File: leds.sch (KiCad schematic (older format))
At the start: 218 parts, among them U10 TLC5955, U11 TLC5955, U12 TLC5955, U13 TLC5955, U14 TLC5955, U15 TLC5955, U4 TLC5955, U5 TLC5955, U6 TLC5955, U7 TLC5955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

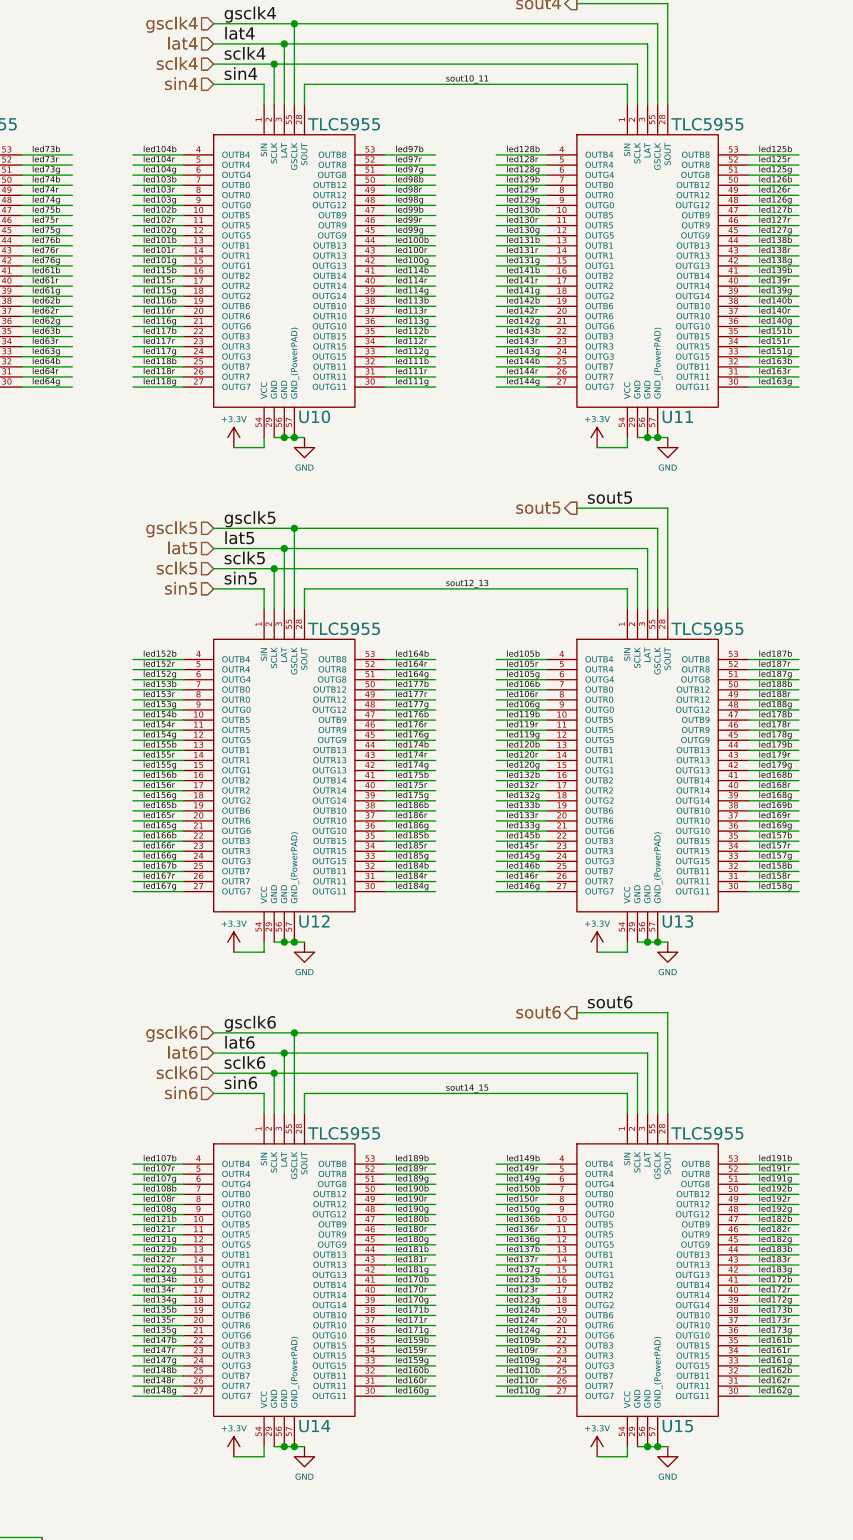
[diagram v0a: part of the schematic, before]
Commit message: Fix LED-mapping for lower half to match upper half.
(In schematics and netlist).
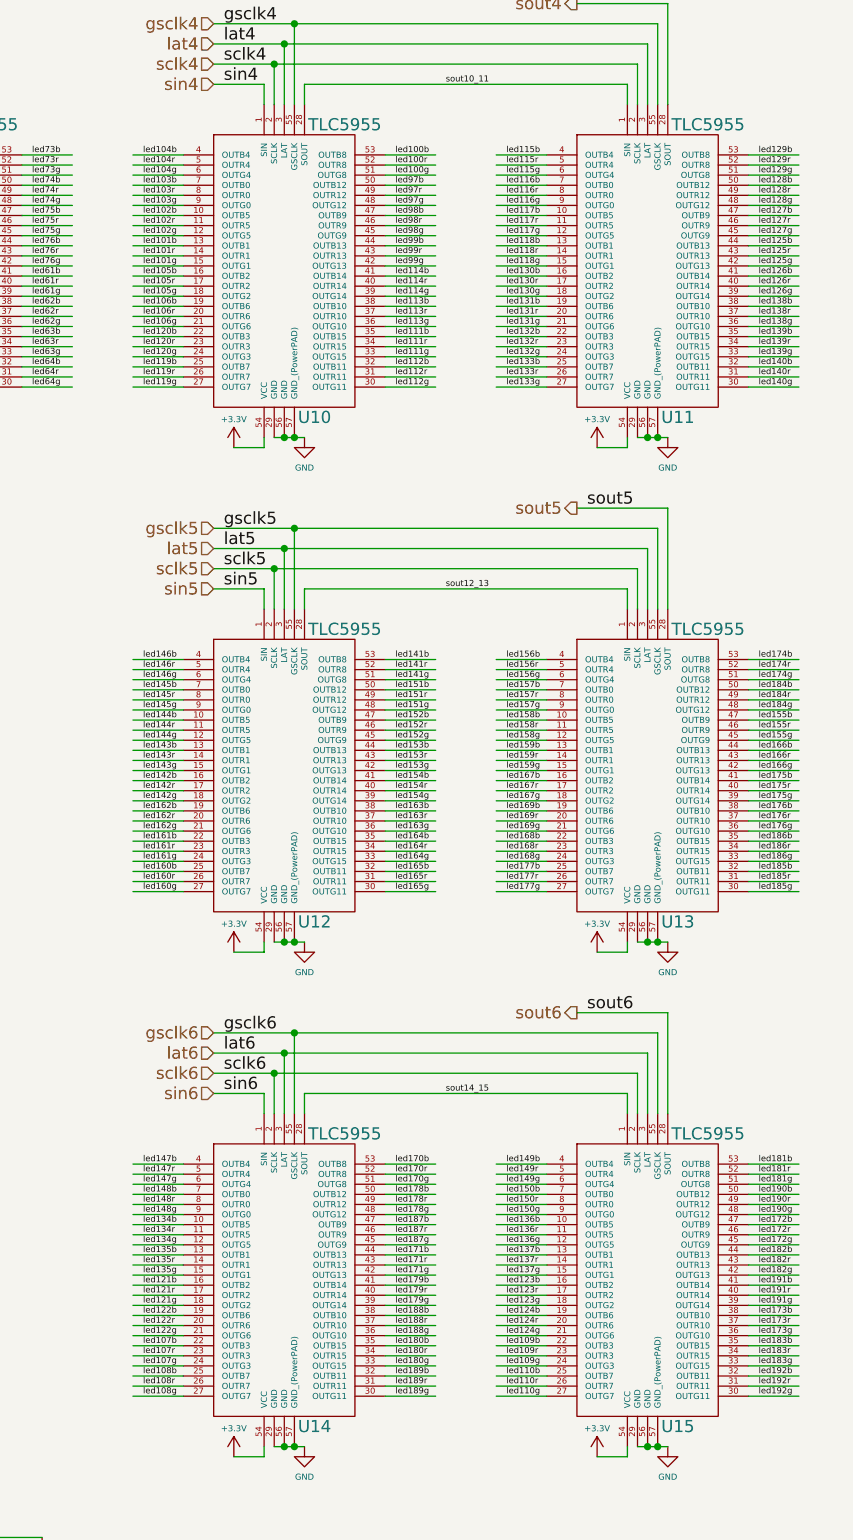
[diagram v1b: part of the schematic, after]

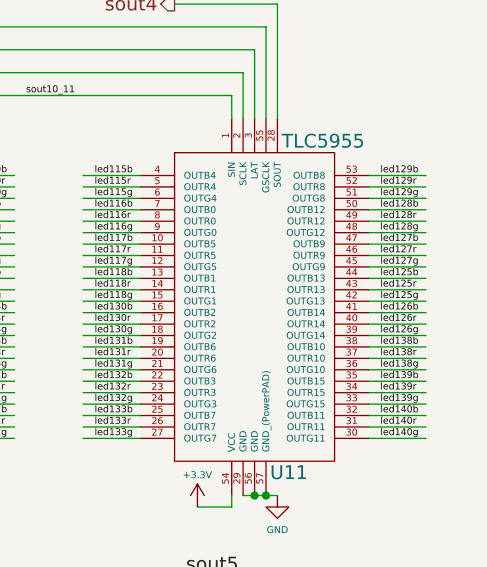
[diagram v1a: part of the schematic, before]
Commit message: Back TLC part of lower half of LEDs routed.
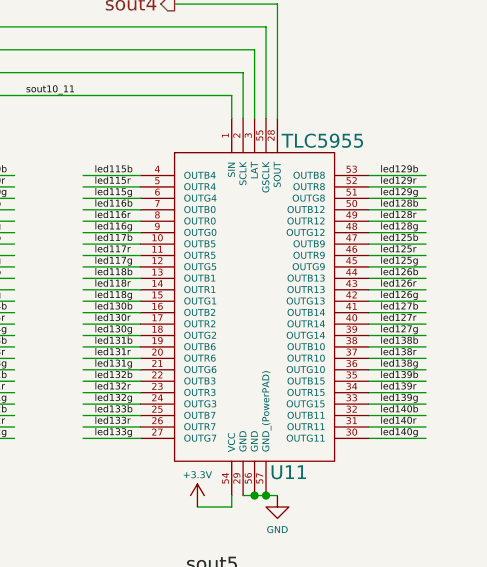
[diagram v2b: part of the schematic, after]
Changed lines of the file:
@@
 led138g
+Wire Wire Line
+	15550 2350 15300 2350
+Wire Wire Line
+	15550 2400 15300 2400
+Wire Wire Line
+	14300 2450 14050 2450
+Text Label 15350 2350 0    30   ~ 0
+led126b
+Text Label 15350 2400 0    30   ~ 0
+led126r
+Text Label 15350 2450 0    30   ~ 0
+led126g
+Wire Wire Line
+	15550 2200 15300 2200
+Wire Wire Line
+	15550 2250 15300 2250
+Wire Wire Line
+	14300 2600 14050 2600
+Text Label 15350 2200 0    30   ~ 0
+led125b
+Text Label 15350 2250 0    30   ~ 0
+led125r
+Text Label 15350 2300 0    30   ~ 0
+led125g
 Wire Wire Line
 	15550 2500 15300 2500
@@
 	15550 2550 15300 2550
 Wire Wire Line
-	14300 2450 14050 2450
+	14300 2750 14050 2750
 Text Label 15350 2500 0    30   ~ 0
-led126b
+led127b
 Text Label 15350 2550 0    30   ~ 0
-led126r
+led127r
 Text Label 15350 2600 0    30   ~ 0
-led126g
-Wire Wire Line
-	15550 2350 15300 2350
-Wire Wire Line
-	15550 2400 15300 2400
-Wire Wire Line
-	14300 2600 14050 2600
-Text Label 15350 2350 0    30   ~ 0
-led125b
-Text Label 15350 2400 0    30   ~ 0
-led125r
-Text Label 15350 2450 0    30   ~ 0
-led125g
-Wire Wire Line
-	15550 2200 15300 2200
-Wire Wire Line
-	15550 2250 15300 2250
-Wire Wire Line
-	14300 2750 14050 2750
-Text Label 15350 2200 0    30   ~ 0
-led127b
-Text Label 15350 2250 0    30   ~ 0
-led127r
-Text Label 15350 2300 0    30   ~ 0
 led127g
 Wire Wire Line

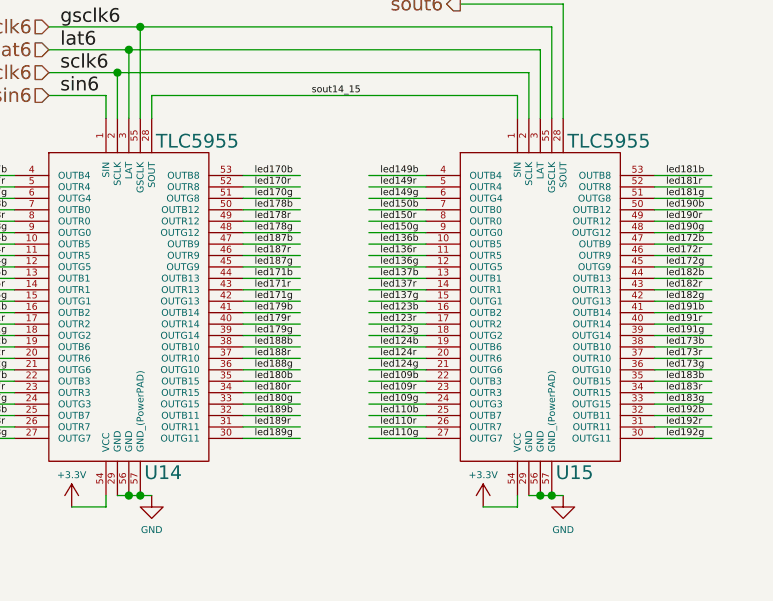
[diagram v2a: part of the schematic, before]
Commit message: Complete routing of LEDs.
Probably a good idea to do some additional cleanup, but it seems
already reasonable.
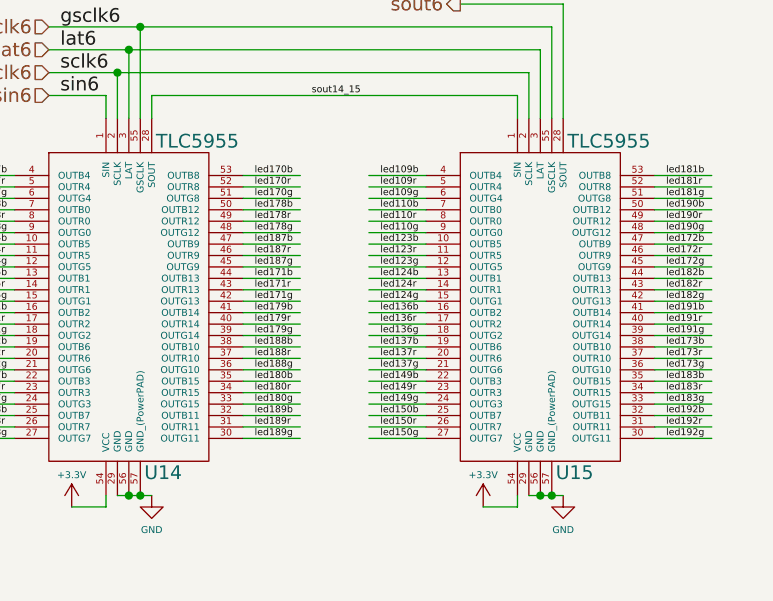
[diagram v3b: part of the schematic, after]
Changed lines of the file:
@@
 $EndComp
+Wire Wire Line
+	14300 7800 14050 7800
+Wire Wire Line
+	14300 7850 14050 7850
+Wire Wire Line
+	14300 7900 14050 7900
+Text Label 14100 7800 0    30   ~ 0
+led149b
+Text Label 14100 7850 0    30   ~ 0
+led149r
+Text Label 14100 7900 0    30   ~ 0
+led149g
+Wire Wire Line
+	14300 7950 14050 7950
+Wire Wire Line
+	14300 8000 14050 8000
+Wire Wire Line
+	14300 7150 14050 7150
+Text Label 14100 7950 0    30   ~ 0
+led150b
+Text Label 14100 8000 0    30   ~ 0
+led150r
+Text Label 14100 8050 0    30   ~ 0
+led150g
+Wire Wire Line
+	14300 7500 14050 7500
+Wire Wire Line
+	14300 7550 14050 7550
+Wire Wire Line
+	14300 7600 14050 7600
+Text Label 14100 7500 0    30   ~ 0
+led136b
+Text Label 14100 7550 0    30   ~ 0
+led136r
+Text Label 14100 7600 0    30   ~ 0
+led136g
+Wire Wire Line
+	14300 7650 14050 7650
+Wire Wire Line
+	14300 7700 14050 7700
+Wire Wire Line
+	14300 7450 14050 7450
+Text Label 14100 7650 0    30   ~ 0
+led137b
+Text Label 14100 7700 0    30   ~ 0
+led137r
+Text Label 14100 7750 0    30   ~ 0
+led137g
+Wire Wire Line
+	14300 7200 14050 7200
+Wire Wire Line
+	14300 7250 14050 7250
+Wire Wire Line
+	14300 7300 14050 7300
+Text Label 14100 7200 0    30   ~ 0
+led123b
+Text Label 14100 7250 0    30   ~ 0
+led123r
+Text Label 14100 7300 0    30   ~ 0
+led123g
+Wire Wire Line
+	14300 7350 14050 7350
+Wire Wire Line
+	14300 7400 14050 7400
+Wire Wire Line
+	14300 7750 14050 7750
+Text Label 14100 7350 0    30   ~ 0
+led124b
+Text Label 14100 7400 0    30   ~ 0
+led124r
+Text Label 14100 7450 0    30   ~ 0
+led124g
 Wire Wire Line
 	14300 6900 14050 6900
@@
 	14300 7000 14050 7000
 Text Label 14100 6900 0    30   ~ 0
-led149b
+led109b
 Text Label 14100 6950 0    30   ~ 0
-led149r
+led109r
 Text Label 14100 7000 0    30   ~ 0
-led149g
+led109g
 Wire Wire Line
 	14300 7050 14050 7050
@@
 	14300 7100 14050 7100
 Wire Wire Line
-	14300 7150 14050 7150
+	14300 8050 14050 8050
 Text Label 14100 7050 0    30   ~ 0
-led150b
+led110b
 Text Label 14100 7100 0    30   ~ 0
-led150r
+led110r
 Text Label 14100 7150 0    30   ~ 0
-led150g
-Wire Wire Line
-	14300 7200 14050 7200
-Wire Wire Line
-	14300 7250 14050 7250
-Wire Wire Line
-	14300 7300 14050 7300
-Text Label 14100 7200 0    30   ~ 0
-led136b
-Text Label 14100 7250 0    30   ~ 0
-led136r
-Text Label 14100 7300 0    30   ~ 0
-led136g
-Wire Wire Line
-	14300 7350 14050 7350
-Wire Wire Line
-	14300 7400 14050 7400
-Wire Wire Line
-	14300 7450 14050 7450
-Text Label 14100 7350 0    30   ~ 0
-led137b
-Text Label 14100 7400 0    30   ~ 0
-led137r
-Text Label 14100 7450 0    30   ~ 0
-led137g
-Wire Wire Line
-	14300 7500 14050 7500
-Wire Wire Line
-	14300 7550 14050 7550
-Wire Wire Line
-	14300 7600 14050 7600
-Text Label 14100 7500 0    30   ~ 0
-led123b
-Text Label 14100 7550 0    30   ~ 0
-led123r
-Text Label 14100 7600 0    30   ~ 0
-led123g
-Wire Wire Line
-	14300 7650 14050 7650
-Wire Wire Line
-	14300 7700 14050 7700
-Wire Wire Line
-	14300 7750 14050 7750
-Text Label 14100 7650 0    30   ~ 0
-led124b
-Text Label 14100 7700 0    30   ~ 0
-led124r
-Text Label 14100 7750 0    30   ~ 0
-led124g
-Wire Wire Line
-	14300 7800 14050 7800
-Wire Wire Line
-	14300 7850 14050 7850
-Wire Wire Line
-	14300 7900 14050 7900
-Text Label 14100 7800 0    30   ~ 0
-led109b
-Text Label 14100 7850 0    30   ~ 0
-led109r
-Text Label 14100 7900 0    30   ~ 0
-led109g
-Wire Wire Line
-	14300 7950 14050 7950
-Wire Wire Line
-	14300 8000 14050 8000
-Wire Wire Line
-	14300 8050 14050 8050
-Text Label 14100 7950 0    30   ~ 0
-led110b
-Text Label 14100 8000 0    30   ~ 0
-led110r
-Text Label 14100 8050 0    30   ~ 0
 led110g
 Wire Wire Line

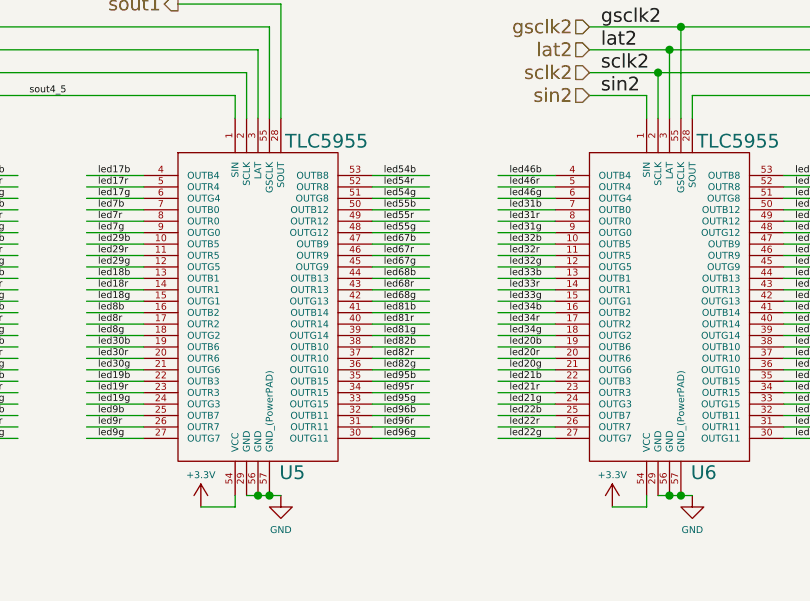
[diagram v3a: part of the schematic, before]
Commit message: Some cleanup of the LED routing.
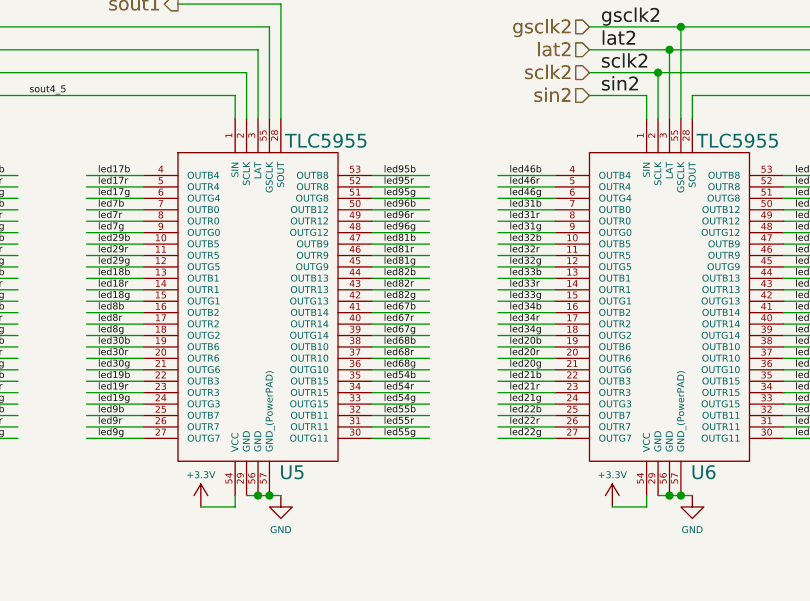
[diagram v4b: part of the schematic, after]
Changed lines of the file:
@@
 	1700 1950 1450 1950
 Wire Wire Line
-	4750 2300 4500 2300
+	4750 2600 4500 2600
 Text Label 1500 1900 0    30   ~ 0
 led27b
@@
 led53g
 Wire Wire Line
-	4750 1900 4500 1900
-Wire Wire Line
-	4750 1950 4500 1950
-Wire Wire Line
-	4750 2000 4500 2000
-Text Label 4550 1900 0    30   ~ 0
+	4750 2800 4500 2800
+Wire Wire Line
+	4750 2850 4500 2850
+Wire Wire Line
+	4750 2900 4500 2900
+Text Label 4550 2800 0    30   ~ 0
 led54b
-Text Label 4550 1950 0    30   ~ 0
+Text Label 4550 2850 0    30   ~ 0
 led54r
-Text Label 4550 2000 0    30   ~ 0
+Text Label 4550 2900 0    30   ~ 0
 led54g
 Wire Wire Line
-	4750 2050 4500 2050
-Wire Wire Line
-	4750 2100 4500 2100
+	4750 2950 4500 2950
+Wire Wire Line
+	4750 3000 4500 3000
 Wire Wire Line
 	7100 2900 6850 2900
-Text Label 4550 2050 0    30   ~ 0
+Text Label 4550 2950 0    30   ~ 0
 led55b
-Text Label 4550 2100 0    30   ~ 0
+Text Label 4550 3000 0    30   ~ 0
 led55r
-Text Label 4550 2150 0    30   ~ 0
+Text Label 4550 3050 0    30   ~ 0
 led55g
 Wire Wire Line
@@
 	10700 2550 10450 2550
 Wire Wire Line
-	4750 2600 4500 2600
+	4750 2300 4500 2300
 Text Label 10500 2500 0    30   ~ 0
 led57b
@@
 led66g
 Wire Wire Line
-	4750 2200 4500 2200
-Wire Wire Line
-	4750 2250 4500 2250
+	4750 2500 4500 2500
+Wire Wire Line
+	4750 2550 4500 2550
 Wire Wire Line
 	10700 2450 10450 2450
-Text Label 4550 2200 0    30   ~ 0
+Text Label 4550 2500 0    30   ~ 0
 led67b
-Text Label 4550 2250 0    30   ~ 0
+Text Label 4550 2550 0    30   ~ 0
 led67r
-Text Label 4550 2300 0    30   ~ 0
+Text Label 4550 2600 0    30   ~ 0
 led67g
 Wire Wire Line
-	4750 2350 4500 2350
-Wire Wire Line
-	4750 2400 4500 2400
+	4750 2650 4500 2650
+Wire Wire Line
+	4750 2700 4500 2700
 Wire Wire Line
 	8900 2450 8650 2450
-Text Label 4550 2350 0    30   ~ 0
+Text Label 4550 2650 0    30   ~ 0
 led68b
-Text Label 4550 2400 0    30   ~ 0
+Text Label 4550 2700 0    30   ~ 0
 led68r
-Text Label 4550 2450 0    30   ~ 0
+Text Label 4550 2750 0    30   ~ 0
 led68g
 Wire Wire Line
@@
 	10150 3000 9900 3000
 Wire Wire Line
-	4750 2900 4500 2900
+	4750 2000 4500 2000
 Text Label 9950 2950 0    30   ~ 0
 led77b
@@
 $EndComp
 Wire Wire Line
-	4750 2500 4500 2500
-Wire Wire Line
-	4750 2550 4500 2550
+	4750 2200 4500 2200
+Wire Wire Line
+	4750 2250 4500 2250
 Wire Wire Line
 	10700 2000 10450 2000
-Text Label 4550 2500 0    30   ~ 0
+Text Label 4550 2200 0    30   ~ 0
 led81b
-Text Label 4550 2550 0    30   ~ 0
+Text Label 4550 2250 0    30   ~ 0
 led81r
-Text Label 4550 2600 0    30   ~ 0
+Text Label 4550 2300 0    30   ~ 0
 led81g
 Wire Wire Line
-	4750 2650 4500 2650
-Wire Wire Line
-	4750 2700 4500 2700
+	4750 2350 4500 2350
+Wire Wire Line
+	4750 2400 4500 2400
 Wire Wire Line
 	10700 2150 10450 2150
-Text Label 4550 2650 0    30   ~ 0
+Text Label 4550 2350 0    30   ~ 0
 led82b
-Text Label 4550 2700 0    30   ~ 0
+Text Label 4550 2400 0    30   ~ 0
 led82r
-Text Label 4550 2750 0    30   ~ 0
+Text Label 4550 2450 0    30   ~ 0
 led82g
 Wire Wire Line
@@
 led94g
 Wire Wire Line
-	4750 2800 4500 2800
-Wire Wire Line
-	4750 2850 4500 2850
+	4750 1900 4500 1900
+Wire Wire Line
+	4750 1950 4500 1950
 Wire Wire Line
 	11950 2300 11700 2300
-Text Label 4550 2800 0    30   ~ 0
+Text Label 4550 1900 0    30   ~ 0
 led95b
-Text Label 4550 2850 0    30   ~ 0
+Text Label 4550 1950 0    30   ~ 0
 led95r
-Text Label 4550 2900 0    30   ~ 0
+Text Label 4550 2000 0    30   ~ 0
 led95g
 Wire Wire Line
-	4750 2950 4500 2950
-Wire Wire Line
-	4750 3000 4500 3000
+	4750 2050 4500 2050
+Wire Wire Line
+	4750 2100 4500 2100
 Wire Wire Line
 	11950 3050 11700 3050
-Text Label 4550 2950 0    30   ~ 0
+Text Label 4550 2050 0    30   ~ 0
 led96b
-Text Label 4550 3000 0    30   ~ 0
+Text Label 4550 2100 0    30   ~ 0
 led96r
-Text Label 4550 3050 0    30   ~ 0
+Text Label 4550 2150 0    30   ~ 0
 led96g
 Wire Wire Line

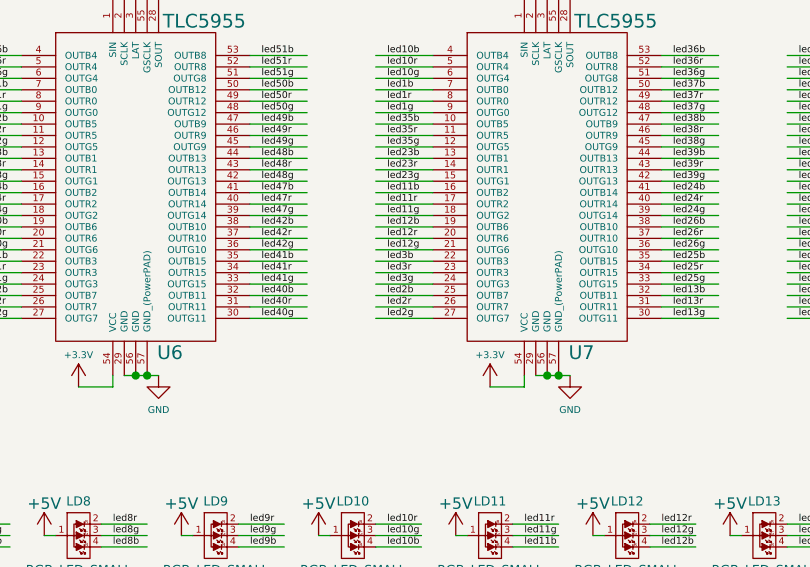
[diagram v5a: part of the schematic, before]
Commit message: Cleanup back routing on U7
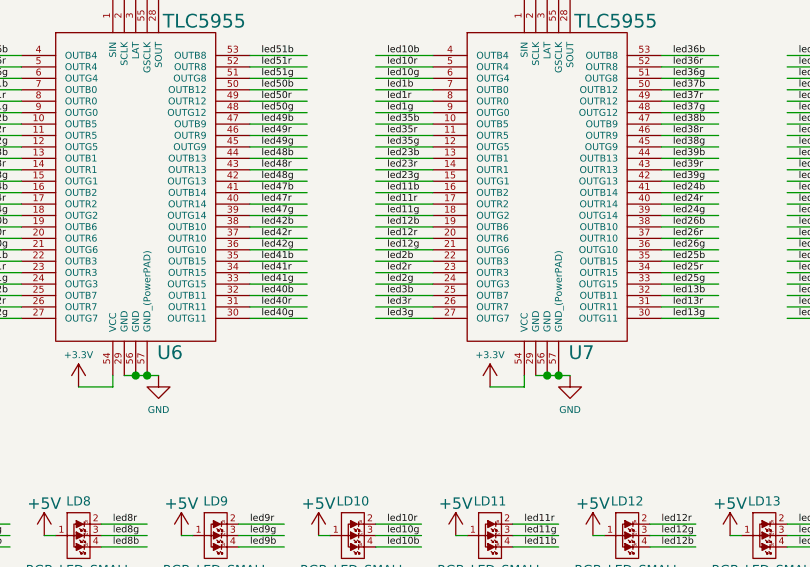
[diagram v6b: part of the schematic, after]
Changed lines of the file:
@@
 led1g
+Wire Wire Line
+	7100 2800 6850 2800
+Wire Wire Line
+	7100 2850 6850 2850
+Wire Wire Line
+	1700 2150 1450 2150
+Text Label 6900 2800 0    30   ~ 0
+led2b
+Text Label 6900 2850 0    30   ~ 0
+led2r
+Text Label 6900 3050 0    30   ~ 0
+led3g
 Wire Wire Line
 	7100 2950 6850 2950
@@
 	7100 3000 6850 3000
 Wire Wire Line
-	1700 2150 1450 2150
+	1700 2300 1450 2300
 Text Label 6900 2950 0    30   ~ 0
-led2b
+led3b
 Text Label 6900 3000 0    30   ~ 0
-led2r
-Text Label 6900 3050 0    30   ~ 0
+led3r
+Text Label 6900 2900 0    30   ~ 0
 led2g
 Wire Wire Line
-	7100 2800 6850 2800
-Wire Wire Line
-	7100 2850 6850 2850
-Wire Wire Line
-	1700 2300 1450 2300
-Text Label 6900 2800 0    30   ~ 0
-led3b
-Text Label 6900 2850 0    30   ~ 0
-led3r
-Text Label 6900 2900 0    30   ~ 0
-led3g
-Wire Wire Line
 	1700 2200 1450 2200
